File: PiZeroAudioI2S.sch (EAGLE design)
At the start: 69 parts, among them CON1 RPI-ZERO, J1 GROVE, J2 2X2HEADER, J3 2X1-LOCKING, J4 GROVE, J5 4X1-LOCKING, Q1 DMG2305UX, U1 TXB0104PWR, U2 LSM6DS33, U3 PCM5101A, U4 DMMT5401, U5 TXS0102, U6 TPA3144D2PWPR

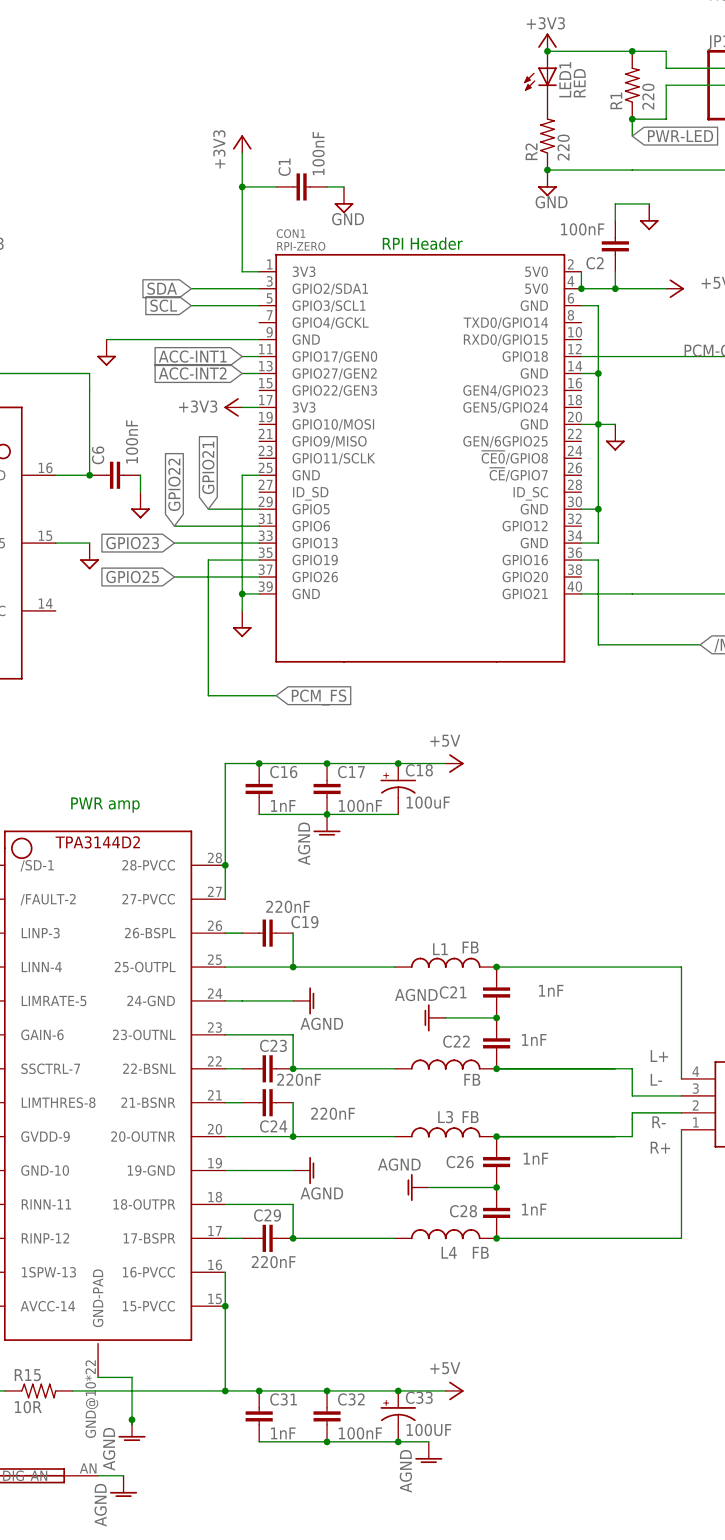
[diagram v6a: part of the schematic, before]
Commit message: changed component values so they are consistent
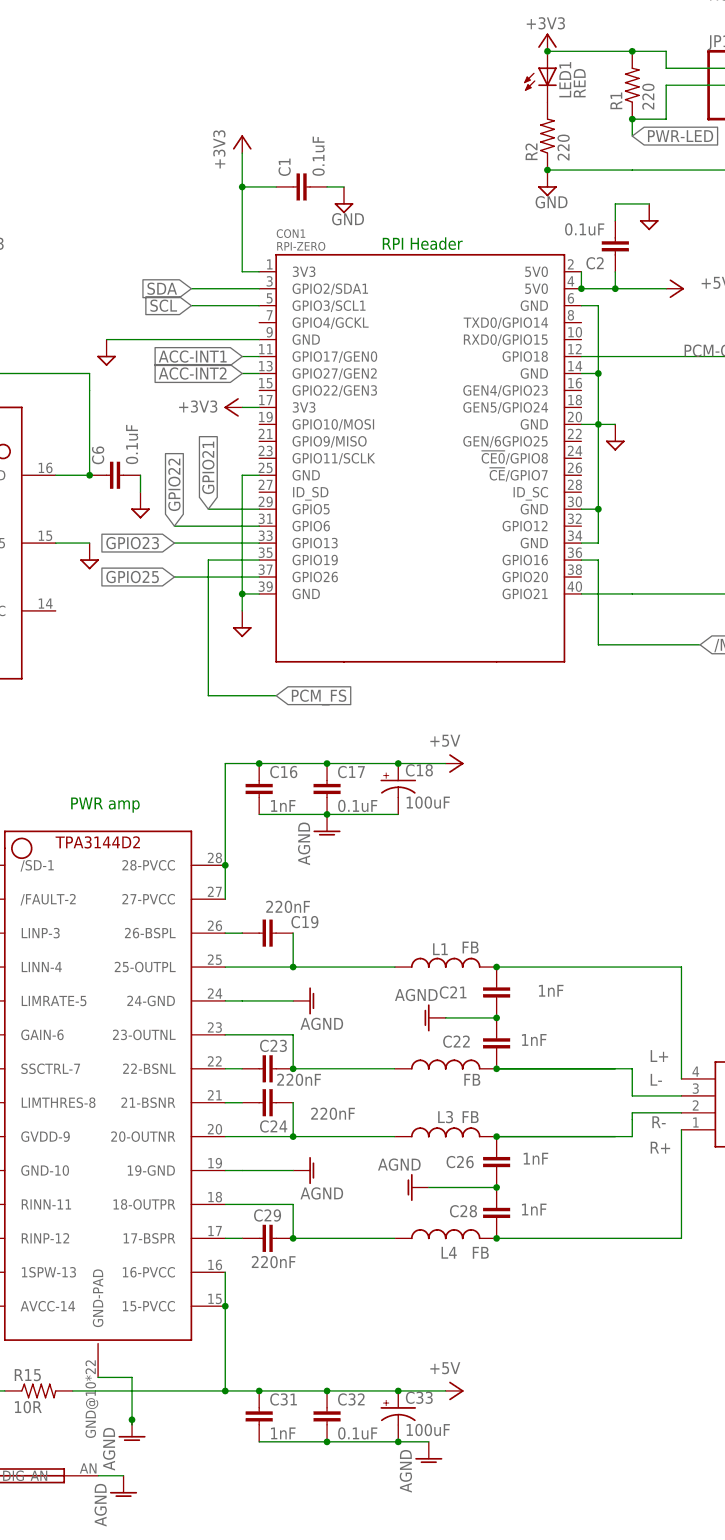
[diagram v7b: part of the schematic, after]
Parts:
- C1, C17, C2, C32, C6: value 100nF -> 0.1uF
- C33: value 100UF -> 100uF
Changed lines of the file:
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@@
 <part name="+3V33" library="supply1" library_urn="urn:adsk.eagle:library:371" deviceset="+3V3" device=""/>
 <part name="U2" library="HappyBrackets" library_urn="urn:adsk.eagle:library:5224691" deviceset="LSM6DS33" device="LGA-16-3X3" package3d_urn="urn:adsk.eagle:package:5224694/1" value="LSM6DS33"/>
-<part name="C6" library="rcl" library_urn="urn:adsk.eagle:library:334" deviceset="C-EU" device="C0603" package3d_urn="urn:adsk.eagle:package:23616/2" value="100nF"/>
+<part name="C6" library="rcl" library_urn="urn:adsk.eagle:library:334" deviceset="C-EU" device="C0603" package3d_urn="urn:adsk.eagle:package:23616/2" value="0.1uF"/>
 <part name="+3V34" library="supply1" library_urn="urn:adsk.eagle:library:371" deviceset="+3V3" device=""/>
-<part name="C1" library="rcl" library_urn="urn:adsk.eagle:library:334" deviceset="C-EU" device="C0603" package3d_urn="urn:adsk.eagle:package:23616/2" value="100nF"/>
+<part name="C1" library="rcl" library_urn="urn:adsk.eagle:library:334" deviceset="C-EU" device="C0603" package3d_urn="urn:adsk.eagle:package:23616/2" value="0.1uF"/>
 <part name="SUPPLY3" library="supply2" library_urn="urn:adsk.eagle:library:372" deviceset="GND" device=""/>
 <part name="R3" library="adafruit" deviceset="R-US_" device="R0603" value="10K"/>
@@
 <part name="SUPPLY10" library="supply2" library_urn="urn:adsk.eagle:library:372" deviceset="GND" device=""/>
 <part name="SUPPLY15" library="supply2" library_urn="urn:adsk.eagle:library:372" deviceset="GND" device=""/>
-<part name="C2" library="rcl" library_urn="urn:adsk.eagle:library:334" deviceset="C-EU" device="C0603" package3d_urn="urn:adsk.eagle:package:23616/2" value="100nF"/>
+<part name="C2" library="rcl" library_urn="urn:adsk.eagle:library:334" deviceset="C-EU" device="C0603" package3d_urn="urn:adsk.eagle:package:23616/2" value="0.1uF"/>
 <part name="SUPPLY4" library="supply2" library_urn="urn:adsk.eagle:library:372" deviceset="GND" device=""/>
 <part name="U1" library="adafruit" deviceset="TXB0104PWR" device="" value="TXB0104PWR"/>
@@
 <part name="U6" library="HappyBrackets" library_urn="urn:adsk.eagle:library:5224691" deviceset="TPA3144D2PWPR" device="" package3d_urn="urn:adsk.eagle:package:39216/1"/>
 <part name="P+4" library="supply1" library_urn="urn:adsk.eagle:library:371" deviceset="+5V" device=""/>
-<part name="C17" library="rcl" library_urn="urn:adsk.eagle:library:334" deviceset="C-EU" device="C0603" package3d_urn="urn:adsk.eagle:package:23616/2" value="100nF"/>
+<part name="C17" library="rcl" library_urn="urn:adsk.eagle:library:334" deviceset="C-EU" device="C0603" package3d_urn="urn:adsk.eagle:package:23616/2" value="0.1uF"/>
 <part name="C18" library="HappyBrackets" library_urn="urn:adsk.eagle:library:5224691" deviceset="CAP-POLARISED" device="" value="100uF"/>
 <part name="R7" library="adafruit" deviceset="R-US_" device="R0603" value="10K"/>
@@
 <part name="R15" library="adafruit" deviceset="R-US_" device="R0603" value="10R"/>
 <part name="P+7" library="supply1" library_urn="urn:adsk.eagle:library:371" deviceset="+5V" device=""/>
-<part name="C32" library="rcl" library_urn="urn:adsk.eagle:library:334" deviceset="C-EU" device="C0603" package3d_urn="urn:adsk.eagle:package:23616/2" value="100nF"/>
-<part name="C33" library="HappyBrackets" library_urn="urn:adsk.eagle:library:5224691" deviceset="CAP-POLARISED" device="" value="100UF"/>
+<part name="C32" library="rcl" library_urn="urn:adsk.eagle:library:334" deviceset="C-EU" device="C0603" package3d_urn="urn:adsk.eagle:package:23616/2" value="0.1uF"/>
+<part name="C33" library="HappyBrackets" library_urn="urn:adsk.eagle:library:5224691" deviceset="CAP-POLARISED" device="" value="100uF"/>
 <part name="C31" library="rcl" library_urn="urn:adsk.eagle:library:334" deviceset="C-EU" device="C0603" package3d_urn="urn:adsk.eagle:package:23616/2" value="1nF"/>
 <part name="L1" library="HappyBrackets" library_urn="urn:adsk.eagle:library:5224691" deviceset="NFZ2MSM" device="L0806" package3d_urn="urn:adsk.eagle:package:32724/1" value="FB"/>

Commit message: Changed Capacitor sizes for tant caps
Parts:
- C11, C13, C15, C18, C33, C4: device HappyBrackets:CAP-POLARISED -> HappyBrackets:CAP-POLARISED1206-POLAR
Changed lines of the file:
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@@
 <part name="P+4" library="supply1" library_urn="urn:adsk.eagle:library:371" deviceset="+5V" device=""/>
 <part name="C17" library="rcl" library_urn="urn:adsk.eagle:library:334" deviceset="C-EU" device="C0603" package3d_urn="urn:adsk.eagle:package:23616/2" value="0.1uF"/>
-<part name="C18" library="HappyBrackets" library_urn="urn:adsk.eagle:library:5224691" deviceset="CAP-POLARISED" device="" value="100uF"/>
+<part name="C18" library="HappyBrackets" library_urn="urn:adsk.eagle:library:5224691" deviceset="CAP-POLARISED" device="1206-POLAR" value="100uF"/>
 <part name="R7" library="adafruit" deviceset="R-US_" device="R0603" value="10K"/>
 <part name="C20" library="rcl" library_urn="urn:adsk.eagle:library:334" deviceset="C-EU" device="C0603" package3d_urn="urn:adsk.eagle:package:23616/2" value="1uF"/>
@@
 <part name="P+7" library="supply1" library_urn="urn:adsk.eagle:library:371" deviceset="+5V" device=""/>
 <part name="C32" library="rcl" library_urn="urn:adsk.eagle:library:334" deviceset="C-EU" device="C0603" package3d_urn="urn:adsk.eagle:package:23616/2" value="0.1uF"/>
-<part name="C33" library="HappyBrackets" library_urn="urn:adsk.eagle:library:5224691" deviceset="CAP-POLARISED" device="" value="100uF"/>
+<part name="C33" library="HappyBrackets" library_urn="urn:adsk.eagle:library:5224691" deviceset="CAP-POLARISED" device="1206-POLAR" value="100uF"/>
 <part name="C31" library="rcl" library_urn="urn:adsk.eagle:library:334" deviceset="C-EU" device="C0603" package3d_urn="urn:adsk.eagle:package:23616/2" value="1nF"/>
 <part name="L1" library="HappyBrackets" library_urn="urn:adsk.eagle:library:5224691" deviceset="NFZ2MSM" device="L0806" package3d_urn="urn:adsk.eagle:package:32724/1" value="FB"/>
@@
 <part name="C9" library="rcl" library_urn="urn:adsk.eagle:library:334" deviceset="C-EU" device="C0603" package3d_urn="urn:adsk.eagle:package:23616/2" value="2.2uF"/>
 <part name="C12" library="rcl" library_urn="urn:adsk.eagle:library:334" deviceset="C-EU" device="C0603" package3d_urn="urn:adsk.eagle:package:23616/2" value="0.1uF"/>
-<part name="C13" library="HappyBrackets" library_urn="urn:adsk.eagle:library:5224691" deviceset="CAP-POLARISED" device="" value="10uF"/>
+<part name="C13" library="HappyBrackets" library_urn="urn:adsk.eagle:library:5224691" deviceset="CAP-POLARISED" device="1206-POLAR" value="10uF"/>
 <part name="AGND4" library="supply1" library_urn="urn:adsk.eagle:library:371" deviceset="AGND" device=""/>
 <part name="AGND5" library="supply1" library_urn="urn:adsk.eagle:library:371" deviceset="AGND" device=""/>
 <part name="SUPPLY14" library="supply2" library_urn="urn:adsk.eagle:library:372" deviceset="GND" device=""/>
-<part name="C15" library="HappyBrackets" library_urn="urn:adsk.eagle:library:5224691" deviceset="CAP-POLARISED" device="" value="10uF"/>
-<part name="C11" library="HappyBrackets" library_urn="urn:adsk.eagle:library:5224691" deviceset="CAP-POLARISED" device="" value="10uF"/>
+<part name="C15" library="HappyBrackets" library_urn="urn:adsk.eagle:library:5224691" deviceset="CAP-POLARISED" device="1206-POLAR" value="10uF"/>
+<part name="C11" library="HappyBrackets" library_urn="urn:adsk.eagle:library:5224691" deviceset="CAP-POLARISED" device="1206-POLAR" value="10uF"/>
 <part name="C10" library="rcl" library_urn="urn:adsk.eagle:library:334" deviceset="C-EU" device="C0603" package3d_urn="urn:adsk.eagle:package:23616/2" value="0.1uF"/>
 <part name="C14" library="rcl" library_urn="urn:adsk.eagle:library:334" deviceset="C-EU" device="C0603" package3d_urn="urn:adsk.eagle:package:23616/2" value="0.1uF"/>
 <part name="+3V37" library="supply1" library_urn="urn:adsk.eagle:library:371" deviceset="+3V3" device=""/>
-<part name="C4" library="HappyBrackets" library_urn="urn:adsk.eagle:library:5224691" deviceset="CAP-POLARISED" device="" value="10uF"/>
+<part name="C4" library="HappyBrackets" library_urn="urn:adsk.eagle:library:5224691" deviceset="CAP-POLARISED" device="1206-POLAR" value="10uF"/>
 <part name="C3" library="rcl" library_urn="urn:adsk.eagle:library:334" deviceset="C-EU" device="C0603" package3d_urn="urn:adsk.eagle:package:23616/2" value="0.1uF"/>
 <part name="AGND1" library="supply1" library_urn="urn:adsk.eagle:library:371" deviceset="AGND" device=""/>
